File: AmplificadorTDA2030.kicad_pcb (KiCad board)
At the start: 2 copper layers, 65.1 x 60.4 mm, 37 parts, among them J1 R_Speaker, J2 SJ1-3523N, J3 DC-005, J4 L_Speaker, U1 TDA2030, U2 TDA2030

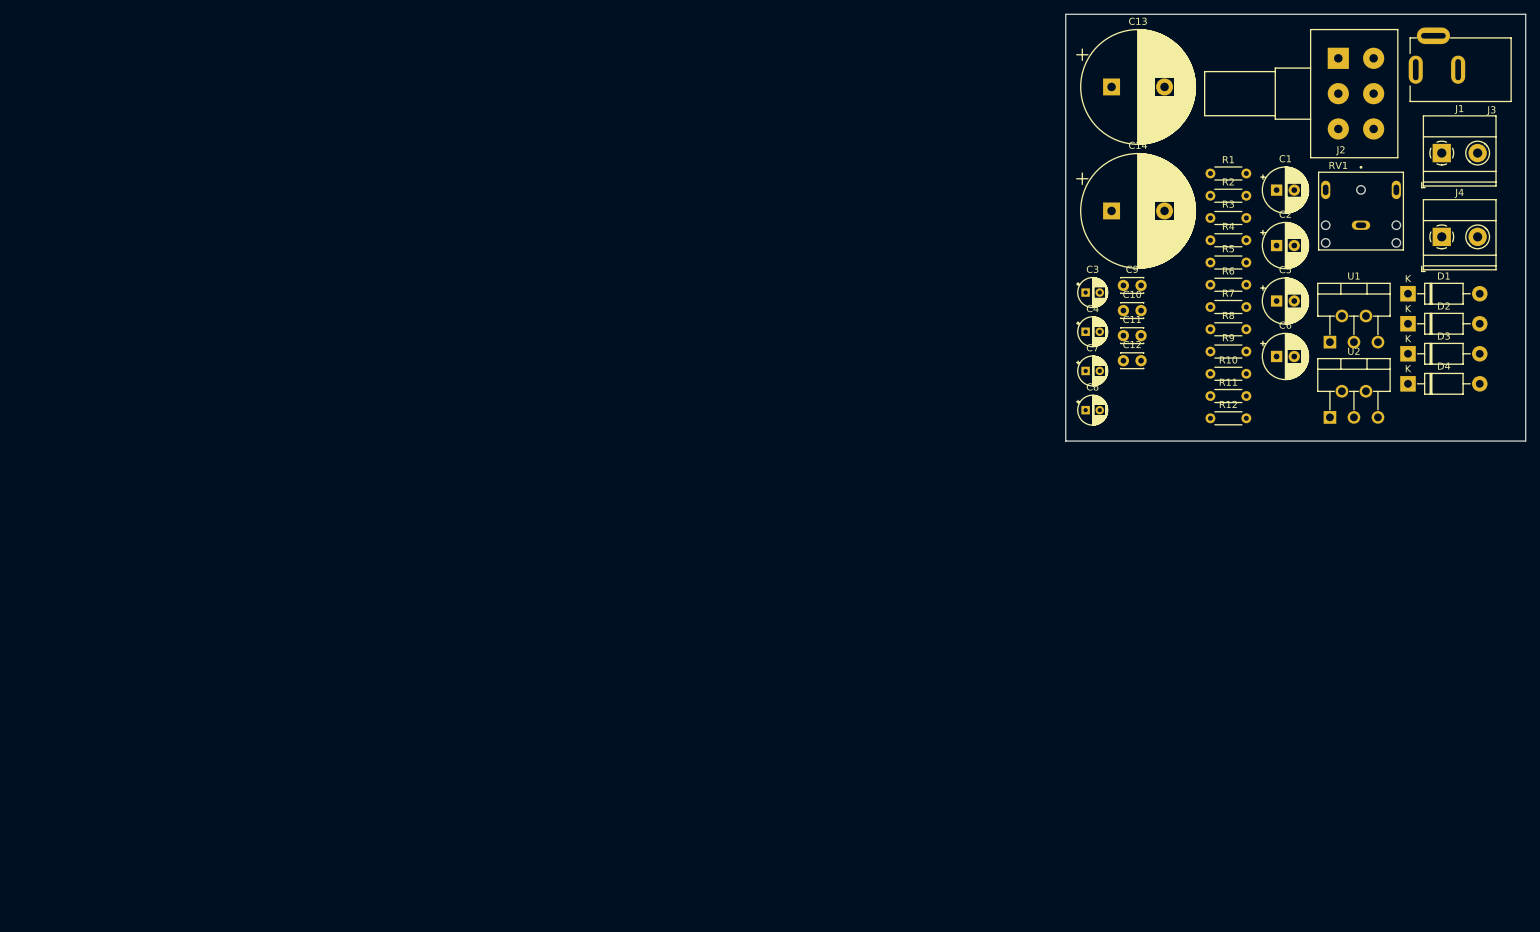
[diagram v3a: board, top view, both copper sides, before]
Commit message: Ruteo de PCB correcto
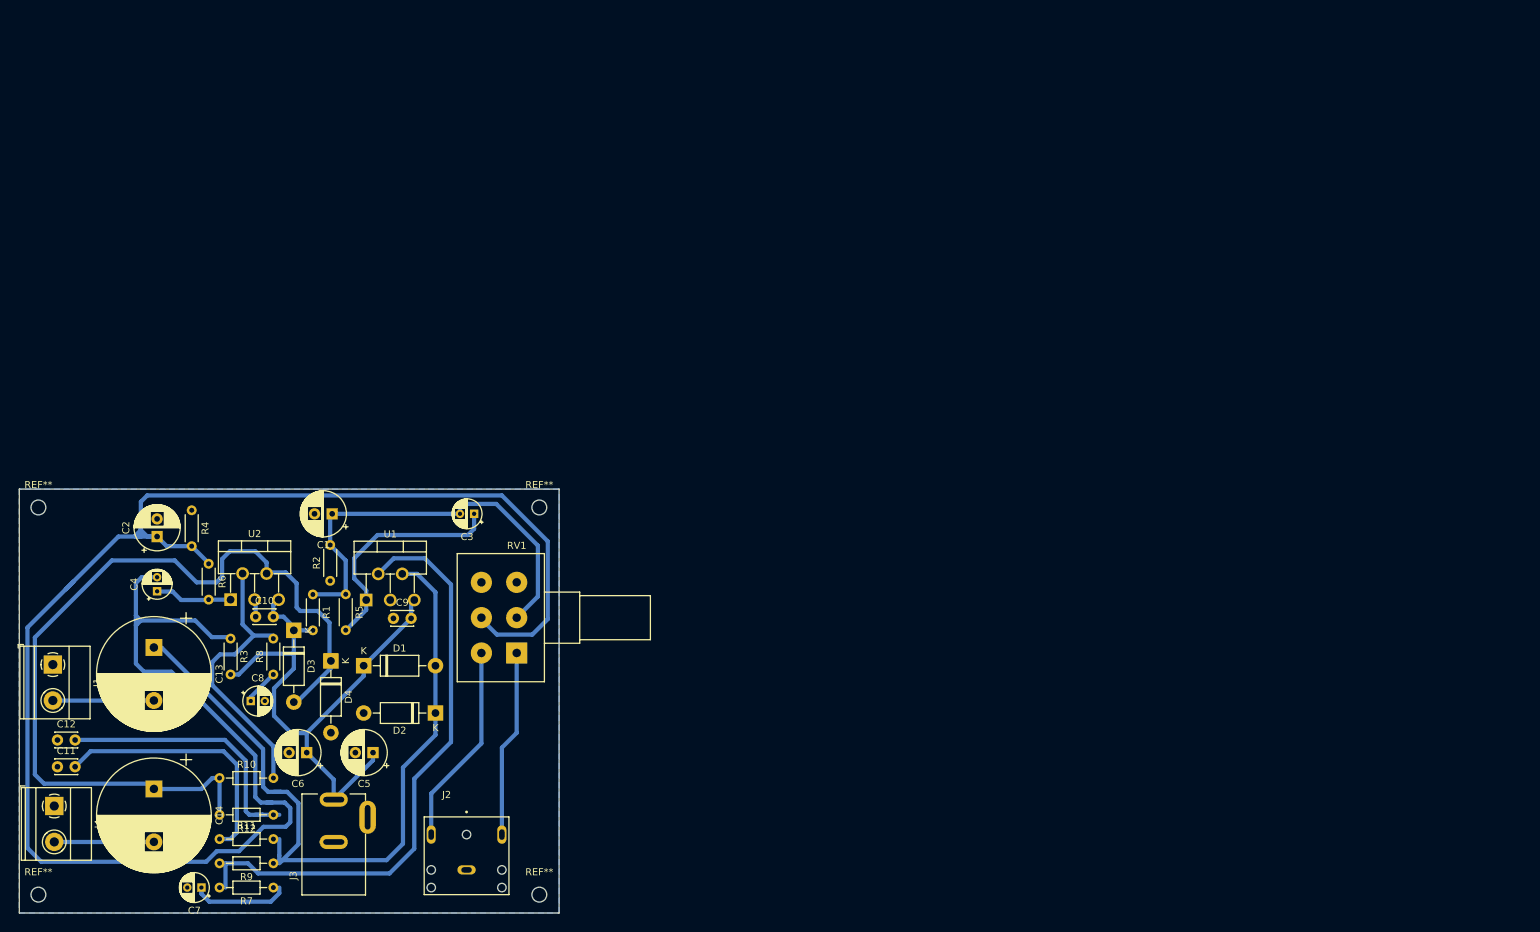
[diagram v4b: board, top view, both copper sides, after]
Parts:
- added REF**: MountingHole_2.1mm, MountingHole:MountingHole_2.1mm, F.Cu at (65.4, 85.2)
- added REF**: MountingHole_2.1mm, MountingHole:MountingHole_2.1mm, F.Cu at (136.3, 85.2)
- added REF**: MountingHole_2.1mm, MountingHole:MountingHole_2.1mm, F.Cu at (136.3, 140.0)
- added REF**: MountingHole_2.1mm, MountingHole:MountingHole_2.1mm, F.Cu at (65.4, 140.0)
- R10, R11, R12, R7, R9: footprint Resistor_THT:R_Axial_DIN0204_L3.6mm_D1.6mm_P5.08mm_Horizontal -> Resistor_THT:R_Axial_DIN0204_L3.6mm_D1.6mm_P7.62mm_Horizontal
- moved J4 212.3 mm to (67.6, 127.5), turned to -90 degrees
- moved J1 209.5 mm to (67.4, 107.4), turned to -90 degrees
- moved J3 188.2 mm to (107.2, 129.1), turned to 90 degrees
- moved C2 163.7 mm to (82.2, 89.3), turned to 90 degrees
- moved C11 162.7 mm to (68.1, 121.9)
- moved D3 162.5 mm to (101.5, 102.6), turned to -90 degrees
- moved C12 160.1 mm to (68.1, 118.1)
- moved C14 158.3 mm to (81.8, 125.0), turned to -90 degrees
- moved U2 157.7 mm to (92.6, 98.2)
- moved D4 157.4 mm to (106.8, 106.9), turned to -90 degrees
- moved C13 157.1 mm to (81.8, 105.0), turned to -90 degrees
- moved D1 156.9 mm to (111.4, 107.6)
- moved J2 156.1 mm to (126.0, 136.5)
- moved R7 156.0 mm to (98.7, 139.0), turned to 180 degrees
- moved R11 153.6 mm to (91.0, 132.1)
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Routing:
- net /L_Input: track 0.00 -> 266.0 mm
- net Net-(D3-A): track 0.00 -> 123.5 mm
- net Net-(D1-A): track 0.00 -> 107.6 mm
- net Net-(U1--): track 0.00 -> 84.5 mm
- net /V+: track 0.00 -> 83.9 mm
- net /R_Input: track 0.00 -> 60.7 mm
- net Net-(U2--): track 0.00 -> 39.6 mm
- net Net-(C12-Pad2): track 0.00 -> 38.5 mm
- net Net-(C11-Pad2): track 0.00 -> 37.0 mm
- net Net-(U1-+): track 0.00 -> 33.6 mm
- net Net-(J2-Pad3): track 0.00 -> 28.6 mm
- net Net-(J2-Pad2): track 0.00 -> 26.6 mm
- net /R_Output: track 0.00 -> 14.3 mm
- net /L_Output: track 0.00 -> 14.1 mm
- net Net-(C7-Pad1): track 0.00 -> 13.7 mm
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- added copper zone on B.Cu, net GND
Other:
- board size 65.1 x 60.4 mm -> 76.4 x 60 mm

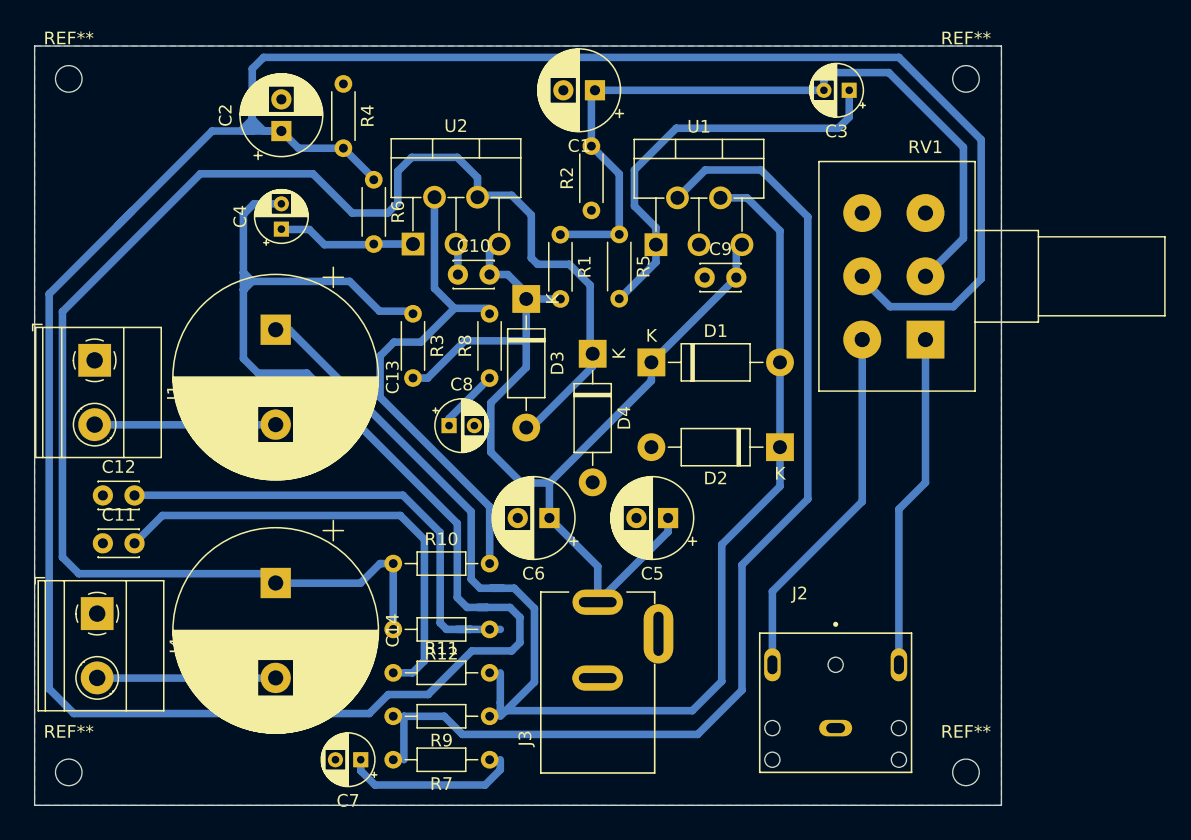
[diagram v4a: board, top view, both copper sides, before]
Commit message: Se agrega LED y Disipadores
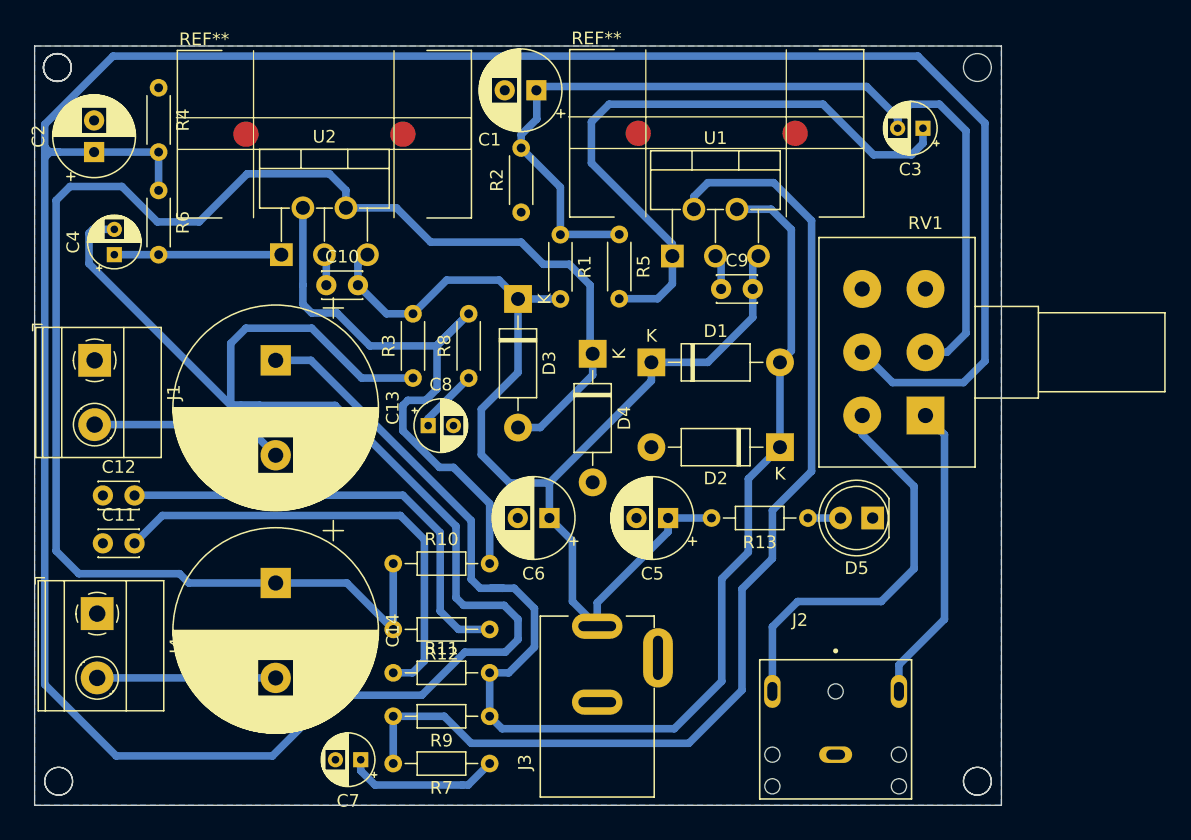
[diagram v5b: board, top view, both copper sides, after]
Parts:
- removed the REF** at (65.4, 85.2)
- removed the REF** at (136.3, 85.2)
- removed the REF** at (136.3, 140.0)
- removed the REF** at (65.4, 140.0)
- added ?: , , F.Cu at (137.2, 84.3)
- added ? (x4): , , F.Cu at (64.5, 84.3)
- added ? (x2): , , F.Cu at (64.6, 140.7)
- added ? (x2): , , F.Cu at (137.2, 140.7)
- added D5: LED, LED_THT:LED_D5.0mm, F.Cu at (128.9, 119.9)
- added R13: 820R, Resistor_THT:R_Axial_DIN0204_L3.6mm_D1.6mm_P7.62mm_Horizontal, F.Cu at (123.8, 119.9)
- added REF**: Heatsink_Fischer_FK24413DPAK_23x13mm, Heatsink:Heatsink_Fischer_FK24413DPAK_23x13mm, F.Cu at (116.6, 89.5)
- added REF**: Heatsink_Fischer_FK24413DPAK_23x13mm, Heatsink:Heatsink_Fischer_FK24413DPAK_23x13mm, F.Cu at (85.6, 89.6)
- moved R6 17.0 mm to (72.5, 94.0)
- moved C2 14.9 mm to (67.4, 91.0)
- moved R4 14.6 mm to (72.5, 85.9)
- moved C4 13.4 mm to (69.0, 99.1)
- moved C10 10.4 mm to (85.8, 101.5)
- moved U2 10.4 mm to (82.2, 99.1)
- moved C3 6.55 mm to (132.9, 89.1)
- moved RV1 6.00 mm to (133.1, 111.8)
- moved R2 5.55 mm to (101.2, 95.7)
- moved R3 5.08 mm to (92.6, 108.8), turned to 90 degrees
- moved C1 4.63 mm to (102.3, 86.1)
- moved C13 2.42 mm to (81.8, 107.4)
- moved J2 2.10 mm to (126.0, 138.6)
- moved J3 1.90 mm to (107.2, 130.9)
- moved C8 1.65 mm to (93.8, 112.6)
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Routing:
- net /L_Input: track 266.0 -> 288.9 mm
- net Net-(U1-+): track 33.6 -> 50.1 mm
- net /R_Input: track 60.7 -> 75.3 mm
- net /V+: track 83.9 -> 96.3 mm
- net Net-(U2--): track 39.6 -> 49.3 mm
- net Net-(J2-Pad3): track 28.6 -> 32.0 mm
- net Net-(D3-A): track 123.5 -> 126.8 mm
- net Net-(J2-Pad2): track 26.6 -> 23.9 mm
- net Net-(D5-A): track 0.00 -> 2.58 mm
- net Net-(C12-Pad2): track 38.5 -> 36.1 mm
- net Net-(U2-+): track 10.9 -> 13.2 mm
- net Net-(C7-Pad1): track 13.7 -> 12.2 mm
- net Net-(D1-A): track 107.6 -> 106.3 mm
- net /R_Output: track 14.3 -> 15.3 mm
- net Net-(U1--): track 84.5 -> 85.3 mm

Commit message: Documentacion Actualizada
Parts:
- removed the ? at (64.5, 84.3) (x3)
- removed the ? at (64.6, 140.7)
- removed the ? at (137.2, 140.7)
- moved ? 0.79 mm to (136.6, 84.8)
- moved ? 0.70 mm to (136.6, 140.4)
- moved ? 0.57 mm to (64.8, 84.8)
- moved ? 0.35 mm to (64.8, 140.4)
- moved D3 0.25 mm to (100.7, 102.6)
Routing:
- net /L_Input: track 288.9 -> 288.1 mm
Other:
- board size 76.4 x 60 mm -> 76 x 60 mm

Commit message: Ruteo
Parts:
- removed the ? at (136.6, 84.8)
- removed the ? at (64.8, 84.8)
- removed the ? at (64.8, 140.4)
- removed the ? at (136.6, 140.4)
- removed the REF** at (116.6, 89.5)
- removed the REF** at (85.6, 89.6)
- added ? (x2): , , F.Cu at (174.5, 70.3)
- added ?: , , F.Cu at (115.0, 120.8)
- added ?: , , F.Cu at (141.4, 70.3)
- added G***: LOGO, Logo_Image:Logo1_Decima 30mm, F.Cu at (184.2, 107.2)
- added REF**: TestPoint_THTPad_D2.0mm_Drill1.0mm, TestPoint:TestPoint_THTPad_D2.0mm_Drill1.0mm, F.Cu at (129.1, 70.3)
- added REF**: TestPoint_THTPad_D2.0mm_Drill1.0mm, TestPoint:TestPoint_THTPad_D2.0mm_Drill1.0mm, F.Cu at (162.2, 70.3)
- added REF**: MountingHole_2.2mm_M2_DIN965_Pad, MountingHole:MountingHole_2.2mm_M2_DIN965_Pad, F.Cu at (184.8, 120.8)
- added REF**: MountingHole_2.2mm_M2_DIN965_Pad, MountingHole:MountingHole_2.2mm_M2_DIN965_Pad, F.Cu at (115.0, 65.9)
- added REF**: MountingHole_2.2mm_M2_DIN965_Pad, MountingHole:MountingHole_2.2mm_M2_DIN965_Pad, F.Cu at (184.8, 65.9)
- R1, R3, R8: footprint Resistor_THT:R_Axial_DIN0204_L3.6mm_D1.6mm_P5.08mm_Horizontal -> Resistor_THT:R_Axial_DIN0204_L3.6mm_D1.6mm_P7.62mm_Horizontal
- moved U1 55.2 mm to (164.9, 80.0)
- moved C9 54.8 mm to (168.3, 82.6)
- moved R1 54.8 mm to (154.2, 75.0)
- moved R5 54.6 mm to (160.3, 79.1)
- moved D3 54.2 mm to (151.4, 83.4)
- moved C1 54.2 mm to (153.1, 66.9)
- moved RV1 53.9 mm to (183.4, 92.6)
- moved D4 53.6 mm to (156.7, 87.4)
- moved R11 53.6 mm to (140.8, 112.2)
- moved R12 53.6 mm to (148.4, 108.8)
- moved R9 53.6 mm to (148.4, 115.7)
- moved R2 53.5 mm to (149.1, 72.0), turned to 0 degrees
- moved R7 53.5 mm to (148.4, 119.6)
- moved C3 53.4 mm to (183.8, 72.8)
- moved C14 53.3 mm to (131.5, 105.8)
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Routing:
- net GND: track 5.46 -> 132.7 mm
- net Net-(D3-A): track 126.8 -> 142.6 mm
- net /V+: track 96.6 -> 107.2 mm
- net /L_Input: track 288.1 -> 277.8 mm
- net Net-(U1-+): track 50.1 -> 59.6 mm
- net Net-(U1--): track 85.3 -> 89.2 mm
- net /R_Input: track 75.1 -> 78.0 mm
- net Net-(J2-Pad3): track 32.0 -> 29.2 mm
- net Net-(U2--): track 49.3 -> 47.2 mm
- net Net-(D5-A): track 2.58 -> 4.59 mm
- net Net-(C8-Pad1): track 5.09 -> 3.81 mm
- net Net-(C12-Pad2): track 36.1 -> 34.9 mm
- net Net-(C11-Pad2): track 37.0 -> 35.9 mm
- net Net-(J2-Pad2): track 23.9 -> 22.9 mm
- net Net-(C7-Pad1): track 12.2 -> 13.0 mm
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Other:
- board size 76 x 60 mm -> 75 x 60 mm
- board text added: "+"
- board text added: "+12VDC"
- board text added: "-"
- board text added: "Audio Input Stereo 3.5mm"
- board text added: "L-Speaker"
- board text added: "R-Speaker"
- board text added: "Volumen"

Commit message: Acutalizacion de Doc
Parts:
- removed the ? at (174.5, 70.3) (x2)
- removed the ? at (141.4, 70.3)
- removed the REF** at (129.1, 70.3)
- removed the REF** at (162.2, 70.3)
- added REF**: Disipador3d, FootPrints-Symbols:Disipador3d, F.Cu at (168.3, 69.5)
- added REF**: Disipador3d, FootPrints-Symbols:Disipador3d, F.Cu at (135.2, 69.4)
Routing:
- net /R_Input: track 78.0 -> 72.1 mm
- net Net-(U1-+): track 59.6 -> 61.2 mm
- net Net-(U1--): track 89.2 -> 88.6 mm
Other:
- outline, holes or cut-outs redrawn
- board text added: "E. Decima"
